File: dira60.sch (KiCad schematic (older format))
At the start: 21 parts, among them U0 ATmega32U4-AU, X0 XTAL_GND

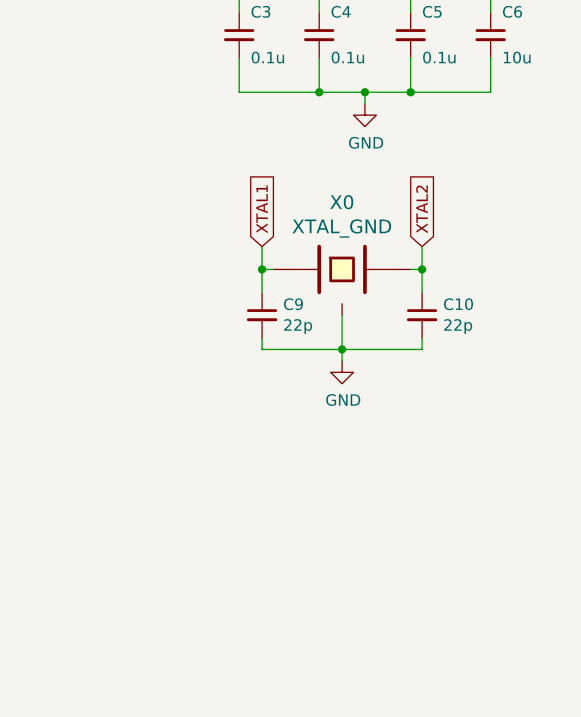
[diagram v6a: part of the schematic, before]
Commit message: Routed CPU's parts
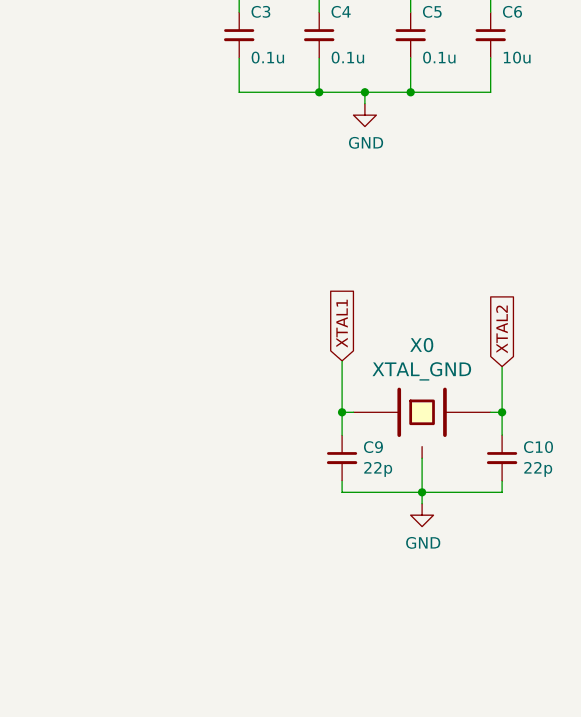
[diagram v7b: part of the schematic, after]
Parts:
- X0: footprint Crystal:Crystal_SMD_3225-4Pin_3.2x2.5mm -> Crystal:Crystal_SMD_SeikoEpson_FA238-4Pin_3.2x2.5mm
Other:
- moved on the sheet: C10, C9, X0
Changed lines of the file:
@@
 Wire Wire Line
 	5500 1000 5500 900
-Text GLabel 9450 4725 1    50   Input ~ 0
-XTAL1
-Text GLabel 10150 4725 1    50   Input ~ 0
-XTAL2
 Wire Wire Line
 	5500 900  6125 900
@@
 L keyboard_parts:XTAL_GND X0
 U 1 1 5C3DE1D0
-P 9800 4825
-F 0 "X0" H 9800 5117 60  0000 C CNN
-F 1 "XTAL_GND" H 9800 5011 60  0000 C CNN
-F 2 "Crystal:Crystal_SMD_3225-4Pin_3.2x2.5mm" H 9800 4825 60  0001 C CNN
-F 3 "" H 9800 4825 60  0000 C CNN
-	1    9800 4825
+P 10150 5450
+F 0 "X0" H 10150 5742 60  0000 C CNN
+F 1 "XTAL_GND" H 10150 5636 60  0000 C CNN
+F 2 "Crystal:Crystal_SMD_SeikoEpson_FA238-4Pin_3.2x2.5mm" H 10150 5450 60  0001 C CNN
+F 3 "" H 10150 5450 60  0000 C CNN
+	1    10150 5450
 	1    0    0    -1
 $EndComp
@@
 L Device:C_Small C9
 U 1 1 5C3DE2B0
-P 9450 5025
-F 0 "C9" H 9542 5071 50  0000 L CNN
-F 1 "22p" H 9542 4980 50  0000 L CNN
-F 2 "Capacitor_SMD:C_0805_2012Metric_Pad1.15x1.40mm_HandSolder" H 9450 5025 50  0001 C CNN
-F 3 "~" H 9450 5025 50  0001 C CNN
-	1    9450 5025
+P 9800 5650
+F 0 "C9" H 9892 5696 50  0000 L CNN
+F 1 "22p" H 9892 5605 50  0000 L CNN
+F 2 "Capacitor_SMD:C_0805_2012Metric_Pad1.15x1.40mm_HandSolder" H 9800 5650 50  0001 C CNN
+F 3 "~" H 9800 5650 50  0001 C CNN
+	1    9800 5650
 	1    0    0    -1
 $EndComp
@@
 L Device:C_Small C10
 U 1 1 5C3DE2EC
-P 10150 5025
-F 0 "C10" H 10242 5071 50  0000 L CNN
-F 1 "22p" H 10242 4980 50  0000 L CNN
-F 2 "Capacitor_SMD:C_0805_2012Metric_Pad1.15x1.40mm_HandSolder" H 10150 5025 50  0001 C CNN
-F 3 "~" H 10150 5025 50  0001 C CNN
-	1    10150 5025
+P 10500 5650
+F 0 "C10" H 10592 5696 50  0000 L CNN
+F 1 "22p" H 10592 5605 50  0000 L CNN
+F 2 "Capacitor_SMD:C_0805_2012Metric_Pad1.15x1.40mm_HandSolder" H 10500 5650 50  0001 C CNN
+F 3 "~" H 10500 5650 50  0001 C CNN
+	1    10500 5650
 	1    0    0    -1
 $EndComp
@@
 L power:GND #PWR0111
 U 1 1 5C3DE405
-P 9800 5225
-F 0 "#PWR0111" H 9800 4975 50  0001 C CNN
-F 1 "GND" H 9805 5052 50  0000 C CNN
-F 2 "" H 9800 5225 50  0001 C CNN
-F 3 "" H 9800 5225 50  0001 C CNN
-	1    9800 5225
-	1    0    0    -1
-$EndComp
-Wire Wire Line
-	9450 4725 9450 4825
-Wire Wire Line
-	9450 4825 9500 4825
-Wire Wire Line
-	9450 4925 9450 4825
-Connection ~ 9450 4825
-Wire Wire Line
-	9450 5125 9450 5175
-Wire Wire Line
-	9450 5175 9800 5175
-Wire Wire Line
-	9800 5175 9800 5225
-Wire Wire Line
-	10150 5125 10150 5175
-Wire Wire Line
-	10150 5175 9800 5175
-Connection ~ 9800 5175
-Wire Wire Line
-	10100 4825 10150 4825
-Wire Wire Line
-	10150 4825 10150 4925
-Wire Wire Line
-	9800 5025 9800 5175
-Wire Wire Line
-	10150 4725 10150 4825
-Connection ~ 10150 4825
-Text GLabel 4900 1950 0    50   Input ~ 0
-XTAL1
-Text GLabel 4900 2150 0    50   Input ~ 0
-XTAL2
+P 10150 5850
+F 0 "#PWR0111" H 10150 5600 50  0001 C CNN
+F 1 "GND" H 10155 5677 50  0000 C CNN
+F 2 "" H 10150 5850 50  0001 C CNN
+F 3 "" H 10150 5850 50  0001 C CNN
+	1    10150 5850
+	1    0    0    -1
+$EndComp
+Wire Wire Line
+	9800 5750 9800 5800
+Wire Wire Line
+	10500 5750 10500 5800
 $Comp
 L power:VCC #PWR0112
@@
 NoConn ~ 2975 5650
 NoConn ~ 2975 5050
+Wire Wire Line
+	10500 5800 10150 5800
+Wire Wire Line
+	10150 5650 10150 5800
+Connection ~ 10150 5800
+Wire Wire Line
+	10150 5800 10150 5850
+Wire Wire Line
+	9800 5800 10150 5800
+Wire Wire Line
+	10450 5450 10500 5450
+Wire Wire Line
+	9850 5450 9800 5450
+Wire Wire Line
+	9800 5550 9800 5450
+Wire Wire Line
+	10500 5550 10500 5450
+Text GLabel 9800 5225 1    50   Input ~ 0
+XTAL1
+Text GLabel 10500 5250 1    50   Input ~ 0
+XTAL2
+Wire Wire Line
+	9800 5225 9800 5450
+Connection ~ 9800 5450
+Wire Wire Line
+	10500 5250 10500 5450
+Connection ~ 10500 5450
+Text GLabel 4900 1950 0    50   Input ~ 0
+XTAL1
+Text GLabel 4900 2150 0    50   Input ~ 0
+XTAL2
 $EndSCHEMATC

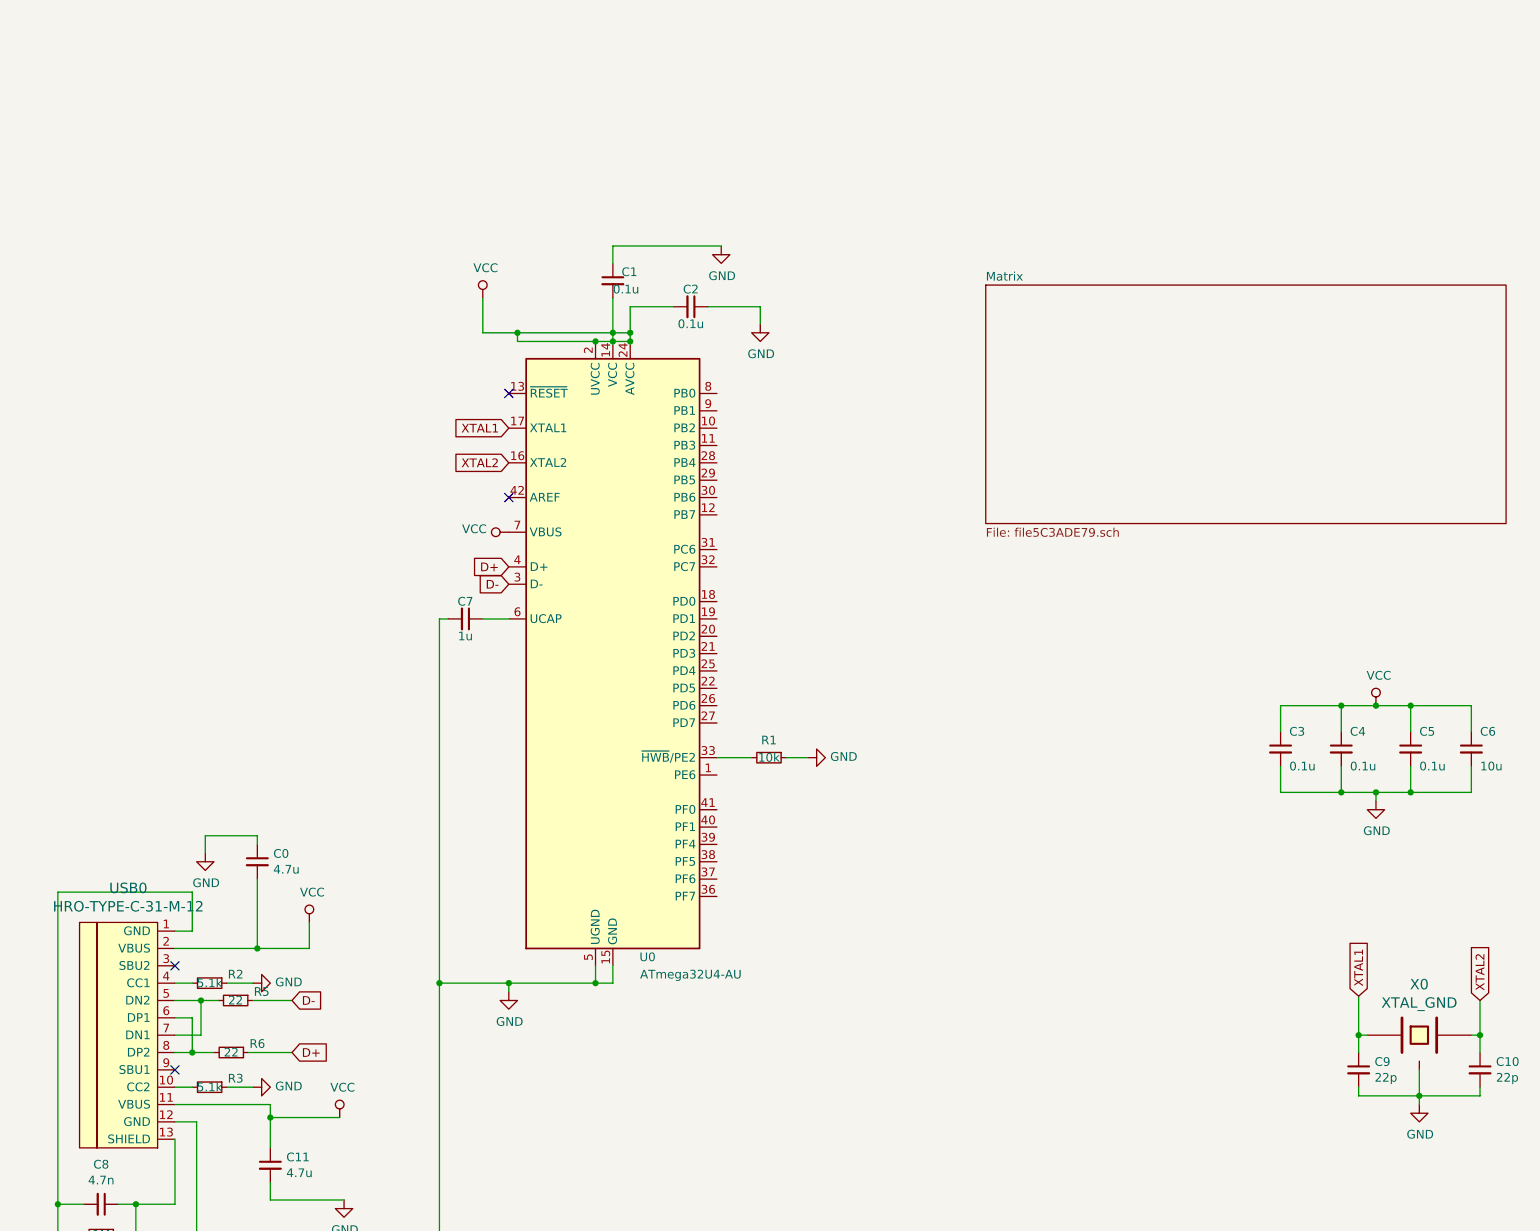
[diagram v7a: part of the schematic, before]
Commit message: Added col 7-14
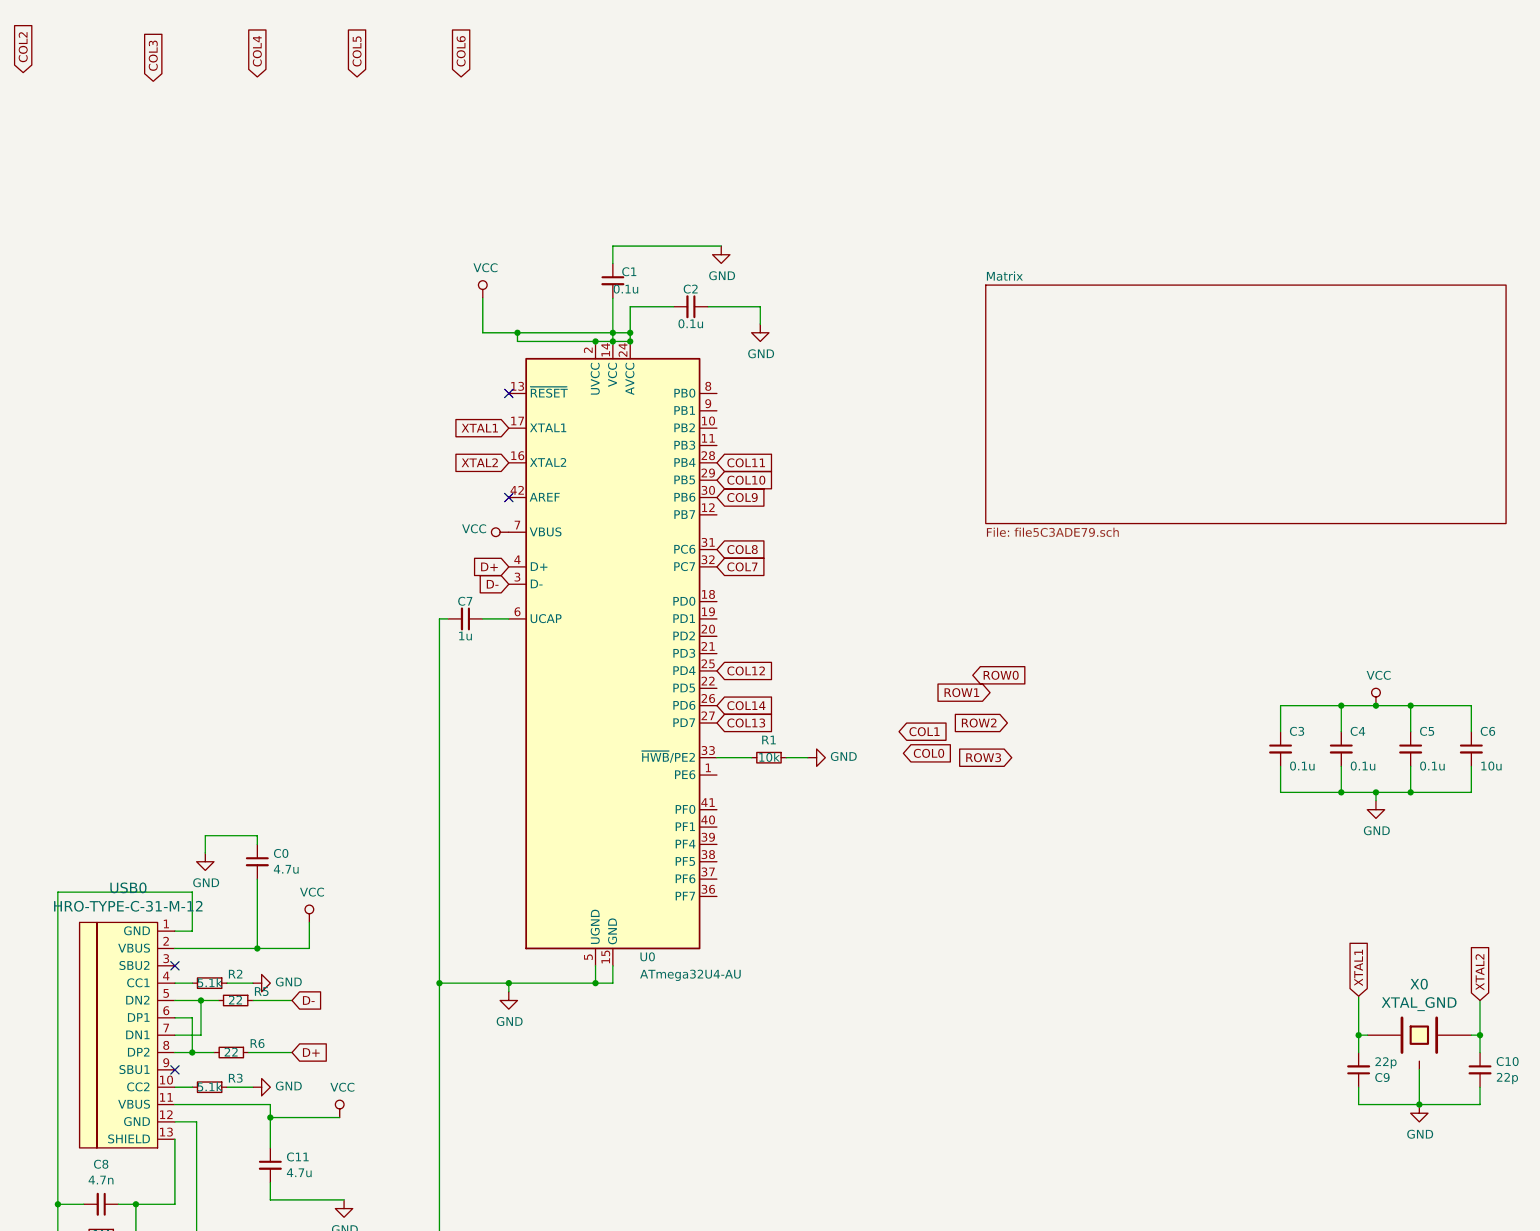
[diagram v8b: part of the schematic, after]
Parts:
- X0: footprint Crystal:Crystal_SMD_SeikoEpson_FA238-4Pin_3.2x2.5mm -> keyboard_parts:FA-238
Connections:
- net GND: now also C9.1; no longer C9.2
- net XTAL1: now also C9.2; no longer C9.1
- net COL12: now reaches U0.25 (PD4)
- net COL14: now reaches U0.26 (PD6)
- net COL13: now reaches U0.27 (PD7)
- net COL11: now reaches U0.28 (PB4)
- net COL10: now reaches U0.29 (PB5)
- net COL9: now reaches U0.30 (PB6)
- net COL8: now reaches U0.31 (PC6)
- net COL7: now reaches U0.32 (PC7)
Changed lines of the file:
@@
 F 0 "X0" H 10150 5742 60  0000 C CNN
 F 1 "XTAL_GND" H 10150 5636 60  0000 C CNN
-F 2 "Crystal:Crystal_SMD_SeikoEpson_FA238-4Pin_3.2x2.5mm" H 10150 5450 60  0001 C CNN
+F 2 "keyboard_parts:FA-238" H 10150 5450 60  0001 C CNN
 F 3 "" H 10150 5450 60  0000 C CNN
 	1    10150 5450
@@
 F 3 "~" H 9800 5650 50  0001 C CNN
 	1    9800 5650
-	1    0    0    -1
+	1    0    0    1
 $EndComp
 $Comp
@@
 	1    0    0    -1
 $EndComp
-Wire Wire Line
-	9800 5750 9800 5800
-Wire Wire Line
-	10500 5750 10500 5800
 $Comp
 L power:VCC #PWR0112
@@
 	4900 5150 4500 5150
 Connection ~ 4900 5150
-Connection ~ 4500 5150
 Connection ~ 5500 1400
 Wire Wire Line
@@
 Wire Wire Line
 	4750 1400 4950 1400
-Wire Wire Line
-	5400 1450 4950 1450
 Wire Wire Line
 	4950 1450 4950 1400
@@
 	5500 1450 5600 1450
 Connection ~ 5500 1450
-Connection ~ 5600 1450
 Wire Wire Line
 	5500 1400 5500 1450
 Wire Wire Line
 	4950 1400 5500 1400
-Wire Wire Line
-	5400 1450 5500 1450
-Connection ~ 5400 1450
 $Comp
 L Type-C:HRO-TYPE-C-31-M-12 USB0
@@
 NoConn ~ 2975 5050
 Wire Wire Line
-	10500 5800 10150 5800
-Wire Wire Line
-	10150 5650 10150 5800
-Connection ~ 10150 5800
-Wire Wire Line
-	10150 5800 10150 5850
-Wire Wire Line
-	9800 5800 10150 5800
-Wire Wire Line
 	10450 5450 10500 5450
 Wire Wire Line
@@
 Text GLabel 4900 2150 0    50   Input ~ 0
 XTAL2
+Text GLabel 7575 3375 2    50   Input ~ 0
+ROW0
+Text GLabel 7675 3475 0    50   Input ~ 0
+ROW1
+Text GLabel 7775 3650 0    50   Input ~ 0
+ROW2
+Text GLabel 7800 3850 0    50   Input ~ 0
+ROW3
+Text GLabel 6100 3550 2    50   Input ~ 0
+COL14
+Text GLabel 6100 3350 2    50   Input ~ 0
+COL12
+Text GLabel 6100 2150 2    50   Input ~ 0
+COL11
+Text GLabel 6100 2250 2    50   Input ~ 0
+COL10
+Text GLabel 6100 2350 2    50   Input ~ 0
+COL9
+Text GLabel 6100 2650 2    50   Input ~ 0
+COL8
+Text GLabel 6100 2750 2    50   Input ~ 0
+COL7
+Text GLabel 4625 -75  1    50   Input ~ 0
+COL6
+Text GLabel 4025 -75  1    50   Input ~ 0
+COL5
+Text GLabel 3450 -75  1    50   Input ~ 0
+COL4
+Text GLabel 2850 -50  1    50   Input ~ 0
+COL3
+Text GLabel 2100 -100 1    50   Input ~ 0
+COL2
+Text GLabel 7150 3700 2    50   Input ~ 0
+COL1
+Text GLabel 7175 3825 2    50   Input ~ 0
+COL0
+Text GLabel 6100 3650 2    50   Input ~ 0
+COL13
+Connection ~ 5400 1450
+Connection ~ 5600 1450
+Wire Wire Line
+	5400 1450 5500 1450
+Wire Wire Line
+	5400 1450 4950 1450
+Connection ~ 4500 5150
+Wire Wire Line
+	10150 5850 10150 5650
+Wire Wire Line
+	10500 5750 10500 5850
+Wire Wire Line
+	10500 5850 10150 5850
+Connection ~ 10150 5850
+Wire Wire Line
+	9800 5750 9800 5850
+Wire Wire Line
+	9800 5850 10150 5850
 $EndSCHEMATC
